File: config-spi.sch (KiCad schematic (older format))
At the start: 44 parts, among them J1 0878311420, J8 61300411121, Q7 BSS138APW, Q8 BSS138APW, U1 XC7K70T-FBG484, U3 S25FL128SAGNFI000

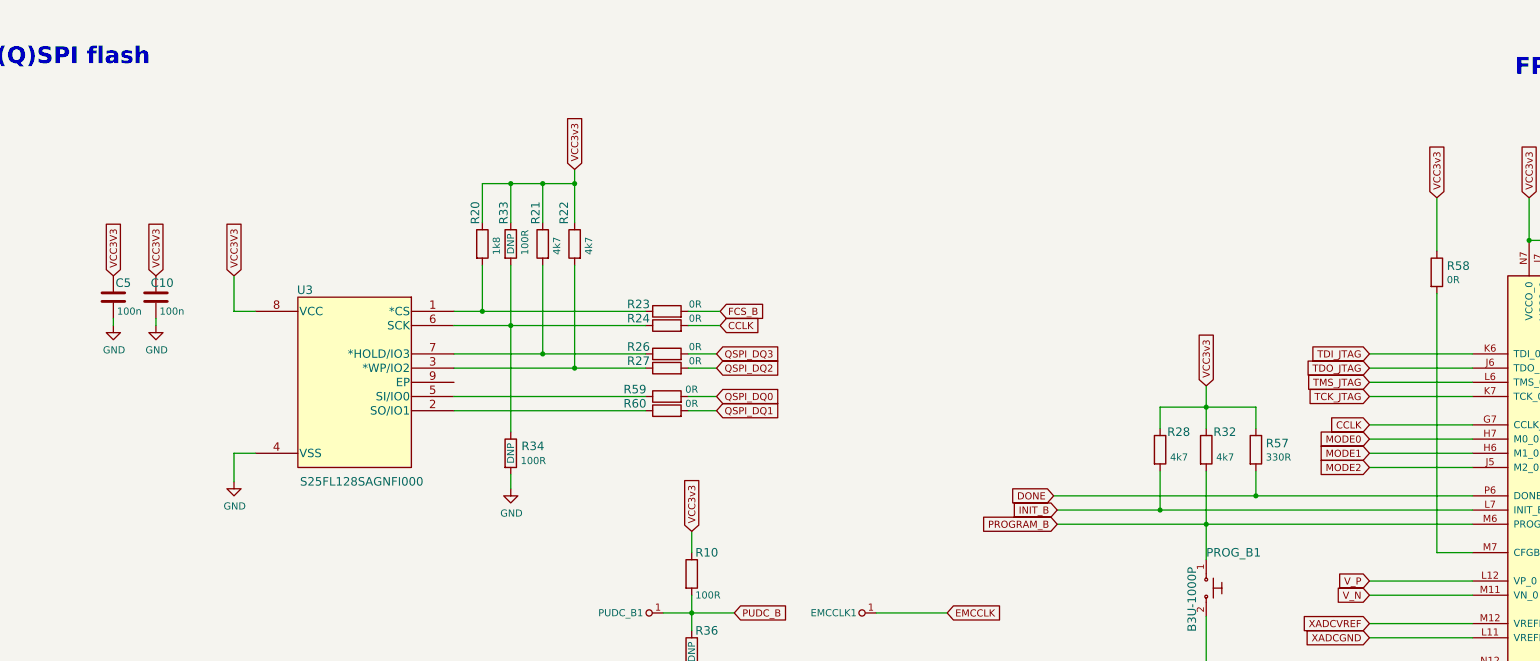
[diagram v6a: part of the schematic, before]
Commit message: Routed configuration block
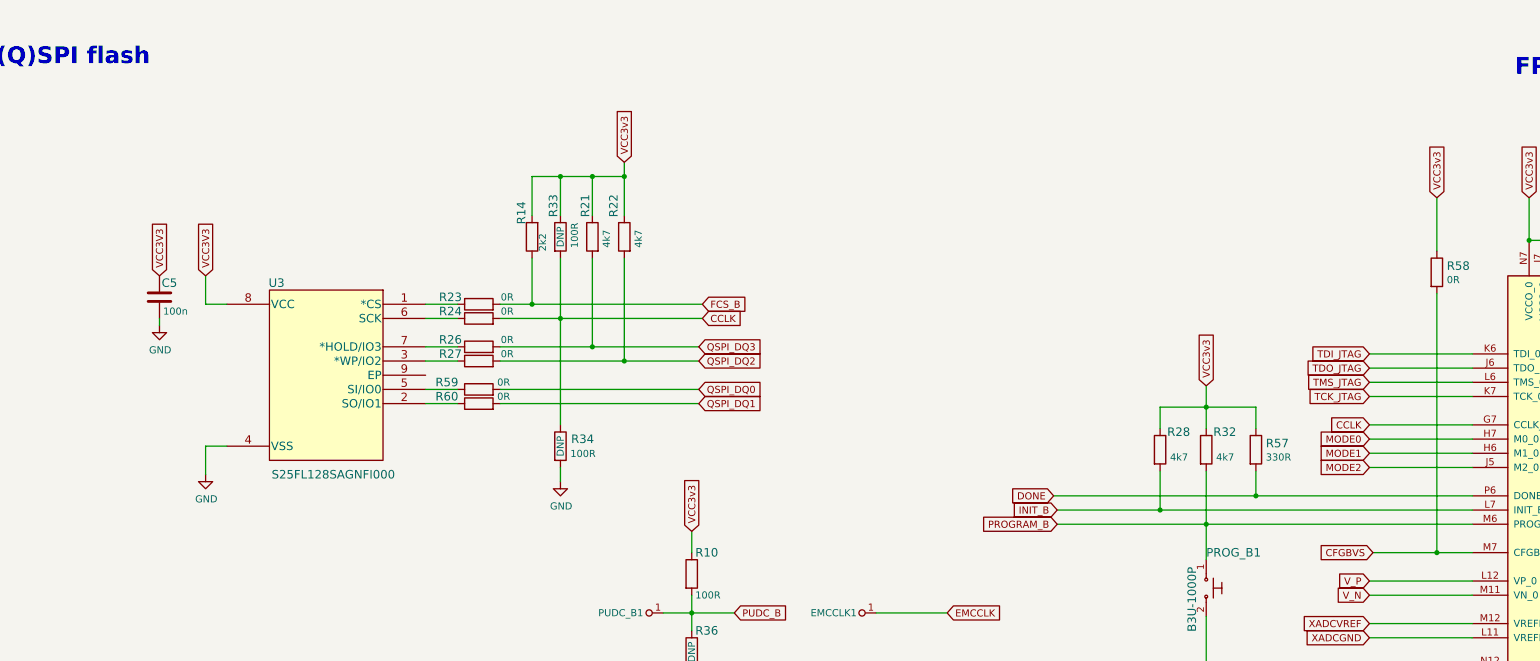
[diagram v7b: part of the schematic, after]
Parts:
- removed C10: C_100n_0402_6V3, lpddr4-test-board-footprints:0402-cap, symbol lpddr4-test-board:C_100n_0402_6V3
- removed R20: R_1k8_0603, lpddr4-test-board-footprints:0603-res, symbol lpddr4-test-board:R_1k8_0603
- added R14: R_2k2_0402, antmicro-footprints:0402-res, symbol antmicroResistors0402:R_2k2_0402
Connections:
- net CCLK: now also R33.2, R34.1
- net FCS_B: now also R14.1
- net QSPI_DQ2: now also R22.2
- net QSPI_DQ3: now also R21.2
- net VCC3v3: now also R14.2
- net at R24.1, U3.6 (SCK): no longer R33.2, R34.1
- net at R27.1, U3.3 (*WP/IO2): no longer R22.2
- net at R26.1, U3.7 (*HOLD/IO3): no longer R21.2
- net CFGBVS: now reaches R58.2, U1.M7 (CFGBVS_0)
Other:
- moved on the sheet: C5, R21, R22, R23, R24, R26, R27, R33, R34, R59, R60, U3

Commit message: Cleanup
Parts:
- removed J1: 0878311420, lpddr4-test-board-footprints:PinHeader_2x7_P2mm_Drill1mm, symbol lpddr4-test-board:0878311420
- added J1: 0878311420, antmicro-footprints:PinHeader_2x7_P2mm_Drill1mm, symbol antmicroRectangularConnectorsHeadersMalePins:0878311420
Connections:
- net GND: now also J1.1, J1.11, J1.13, J1.3, J1.5, J1.7, J1.9
- net TCK_JTAG: now also J1.6
- net TDI_JTAG: now also J1.10
- net TDO_JTAG: now also J1.8
- net TMS_JTAG: now also J1.4
- net VCC3v3: now also J1.2
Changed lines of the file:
@@
 Text Notes 4550 8525 0    118  ~ 24
 STATUS LEDs
-$Comp
-L lpddr4-test-board:0878311420 J1
-U 1 1 5FB8277B
-P 1250 9675
-F 0 "J1" H 1250 10200 50  0000 C CNN
-F 1 "0878311420" H 1250 10109 50  0000 C CNN
-F 2 "lpddr4-test-board-footprints:PinHeader_2x7_P2mm_Drill1mm" H 1450 9875 60  0001 L CNN
-F 3 "https://www.molex.com/pdm_docs/sd/878311420_sd.pdf" H 1450 9975 60  0001 L CNN
-F 4 "0878311420" H 1450 10175 60  0001 L CNN "MPN"
-F 5 "Molex" H 1450 10775 60  0001 L CNN "Manufacturer"
-	1    1250 9675
-	1    0    0    -1
-$EndComp
 Wire Wire Line
 	1450 9375 1625 9375
@@
 Wire Wire Line
 	5050 3250 5050 3525
+$Comp
+L antmicroRectangularConnectorsHeadersMalePins:0878311420 J1
+U 1 1 617E9509
+P 1250 9675
+F 0 "J1" H 1250 10200 50  0000 C CNN
+F 1 "0878311420" H 1250 10109 50  0000 C CNN
+F 2 "antmicro-footprints:PinHeader_2x7_P2mm_Drill1mm" H 1450 9875 60  0001 L CNN
+F 3 "https://www.molex.com/pdm_docs/sd/878311420_sd.pdf" H 1450 9975 60  0001 L CNN
+F 4 "0878311420" H 1450 10175 60  0001 L CNN "MPN"
+F 5 "Molex" H 1450 10775 60  0001 L CNN "Manufacturer"
+	1    1250 9675
+	1    0    0    -1
+$EndComp
 $EndSCHEMATC
